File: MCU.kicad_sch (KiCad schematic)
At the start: 1 part, among them U16 STM32F303VETx

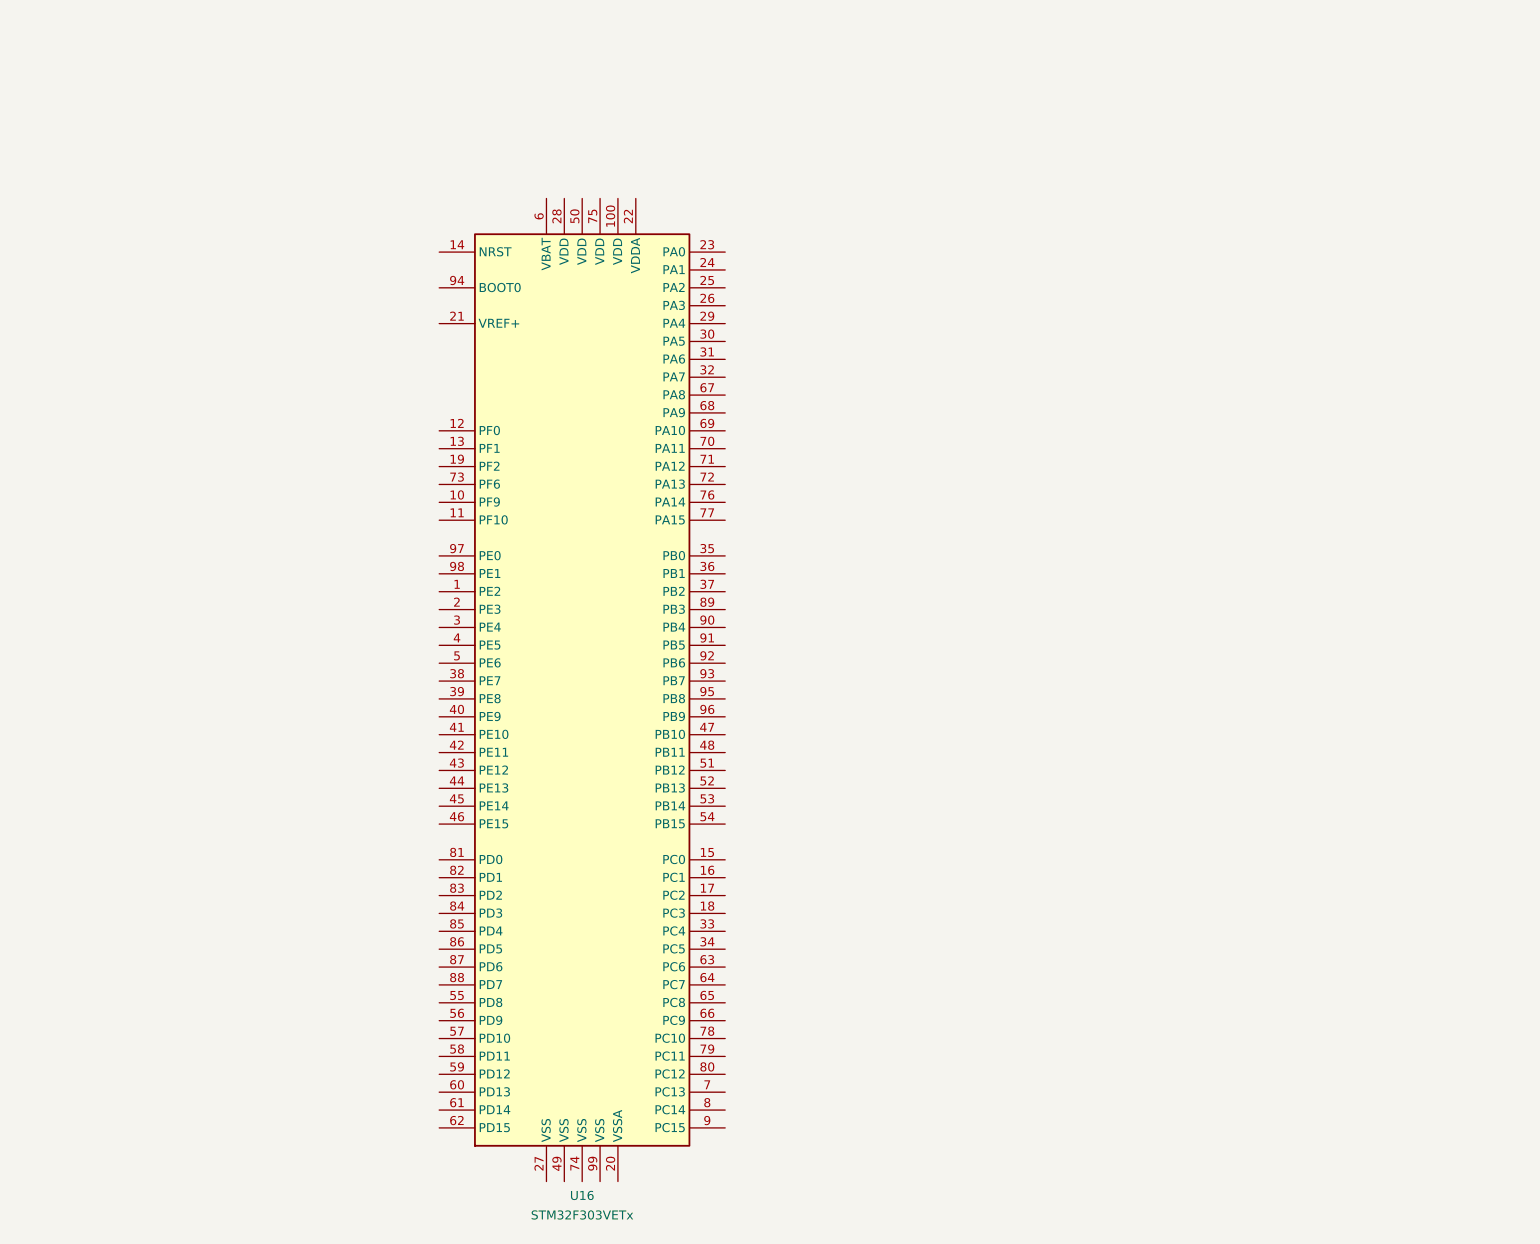
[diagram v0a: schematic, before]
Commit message: Initial layout and all parts added. Some pins still not connected to power
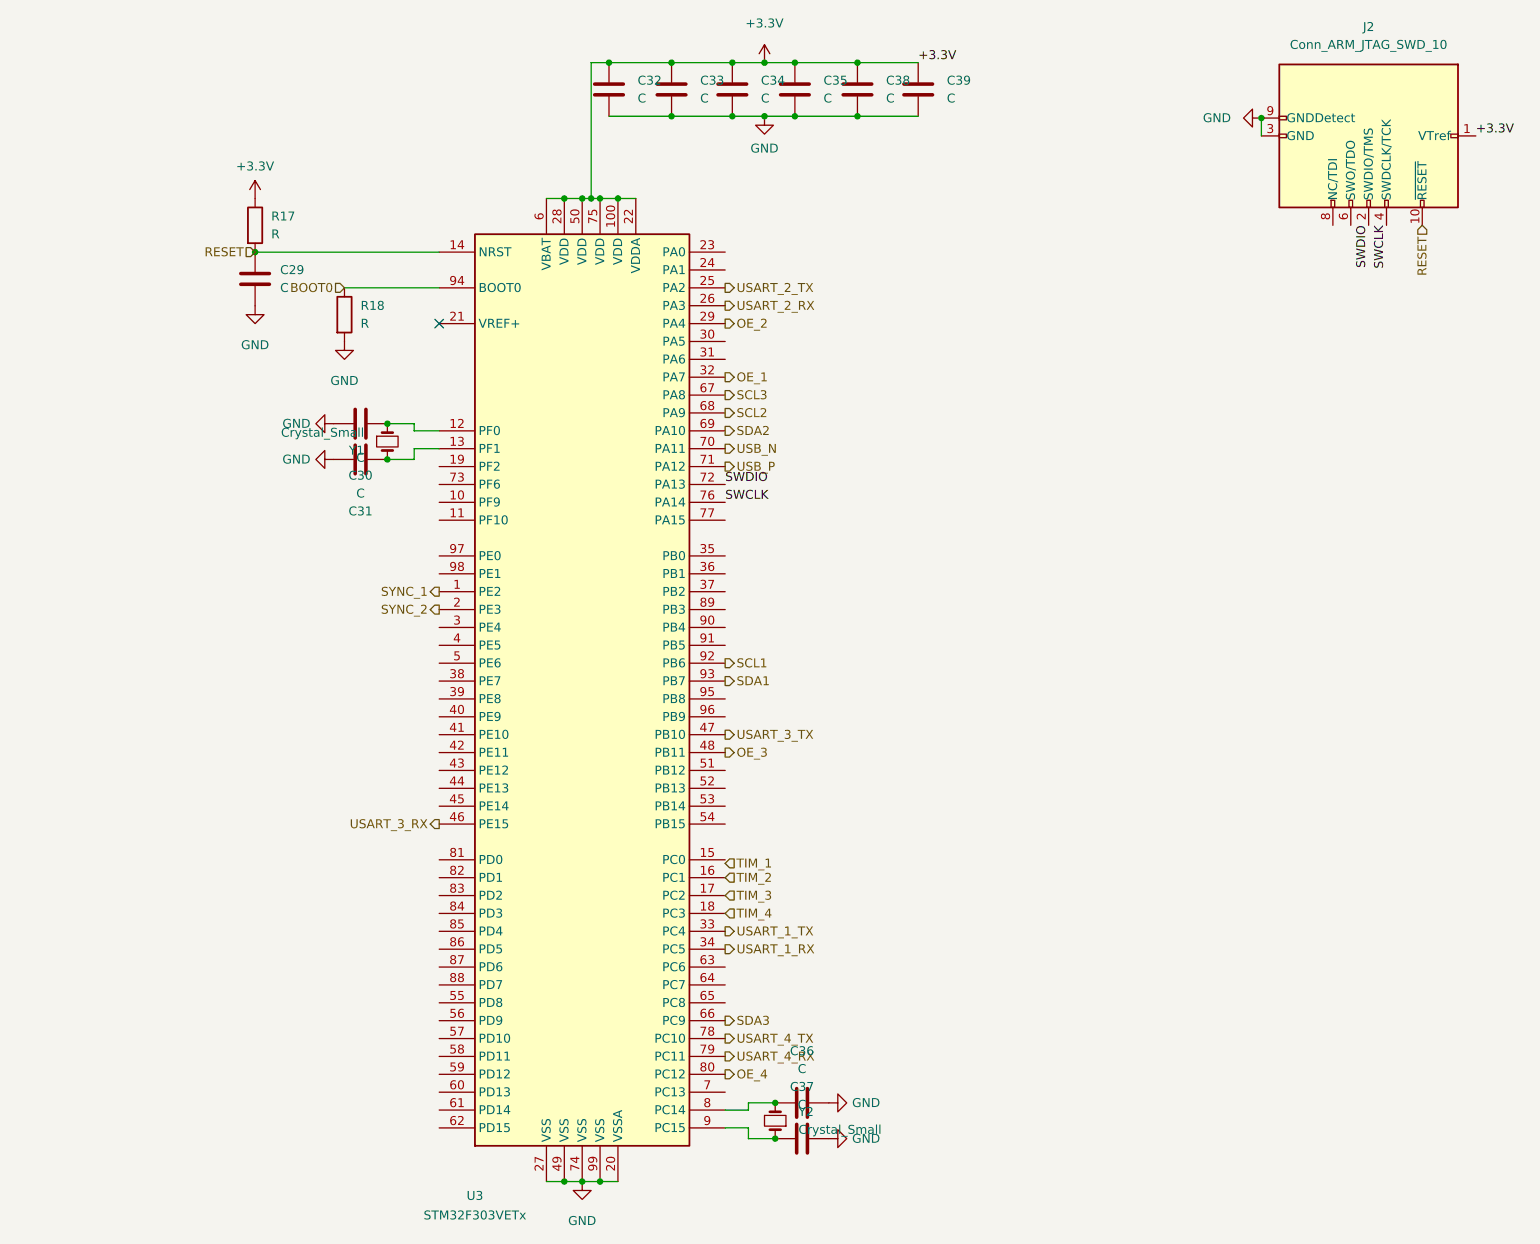
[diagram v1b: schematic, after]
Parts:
- added C29, C30, C31, C32, C33, C34, C35, C36, C37, C38, C39: C, Capacitor_SMD:C_0402_1005Metric, symbol Device:C
- added J2: Conn_ARM_JTAG_SWD_10, Connector_PinHeader_1.27mm:PinHeader_2x05_P1.27mm_Vertical_SMD, symbol Connector:Conn_ARM_JTAG_SWD_10
- added R17, R18: R, Resistor_SMD:R_0402_1005Metric, symbol Device:R
- added Y1, Y2: Crystal_Small, Crystal:Crystal_SMD_2012-2Pin_2.0x1.2mm, symbol Device:Crystal_Small
- renumbered U16 to U3
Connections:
- net SYNC_1: now reaches U3.1 (PE2)
- net +3V3: now reaches U3.100 (VDD)
- net +3V3: now also U3.22 (VDDA), U3.28 (VDD), U3.50 (VDD), U3.6 (VBAT), U3.75 (VDD), C32.1, C33.1, C34.1, C35.1, C38.1, C39.1, J2.1 (VTref), R17.1
- net at U3.12 (PF0): now also C30.1, Y1.1
- net at U3.13 (PF1): now also C31.1, Y1.2
- net RESET: now reaches U3.14 (NRST)
- net RESET: now also C29.1, J2.10 (~{RESET}), R17.2
- net TIM_2: now reaches U3.16 (PC1)
- net TIM_3: now reaches U3.17 (PC2)
- net TIM_4: now reaches U3.18 (PC3)
- net SYNC_2: now reaches U3.2 (PE3)
- net GND: now reaches U3.20 (VSSA)
- net GND: now also U3.27 (VSS), U3.49 (VSS), U3.74 (VSS), U3.99 (VSS), C29.2, C30.2, C31.2, C32.2, C33.2, C34.2, C35.2, C36.2, C37.2, C38.2, C39.2, J2.3 (GND), J2.5 (GND), J2.9 (GNDDetect), R18.2
- net USART_2_TX: now reaches U3.25 (PA2)
- net USART_2_RX: now reaches U3.26 (PA3)
- net OE_2: now reaches U3.29 (PA4)
- net OE_1: now reaches U3.32 (PA7)
- net USART_1_TX: now reaches U3.33 (PC4)
- net USART_1_RX: now reaches U3.34 (PC5)
- net USART_3_RX: now reaches U3.46 (PE15)
- net USART_3_TX: now reaches U3.47 (PB10)
- net OE_3: now reaches U3.48 (PB11)
- net SDA3: now reaches U3.66 (PC9)
- net SCL3: now reaches U3.67 (PA8)
- net SCL2: now reaches U3.68 (PA9)
- net SDA2: now reaches U3.69 (PA10)
- net USB_N: now reaches U3.70 (PA11)
- net USB_P: now reaches U3.71 (PA12)
- net SWDIO: now reaches U3.72 (PA13)
- net SWDIO: now also J2.2 (SWDIO/TMS)
- net SWCLK: now reaches U3.76 (PA14)
- net SWCLK: now also J2.4 (SWDCLK/TCK)
- net USART_4_TX: now reaches U3.78 (PC10)
- net USART_4_RX: now reaches U3.79 (PC11)
- net at U3.8 (PC14): now also C36.1, Y2.2
- net OE_4: now reaches U3.80 (PC12)
- net at U3.9 (PC15): now also C37.1, Y2.1
- net SCL1: now reaches U3.92 (PB6)
- net SDA1: now reaches U3.93 (PB7)
- net BOOT0: now reaches U3.94 (BOOT0)
- net BOOT0: now also R18.1
- no-connect marks 0 -> 1

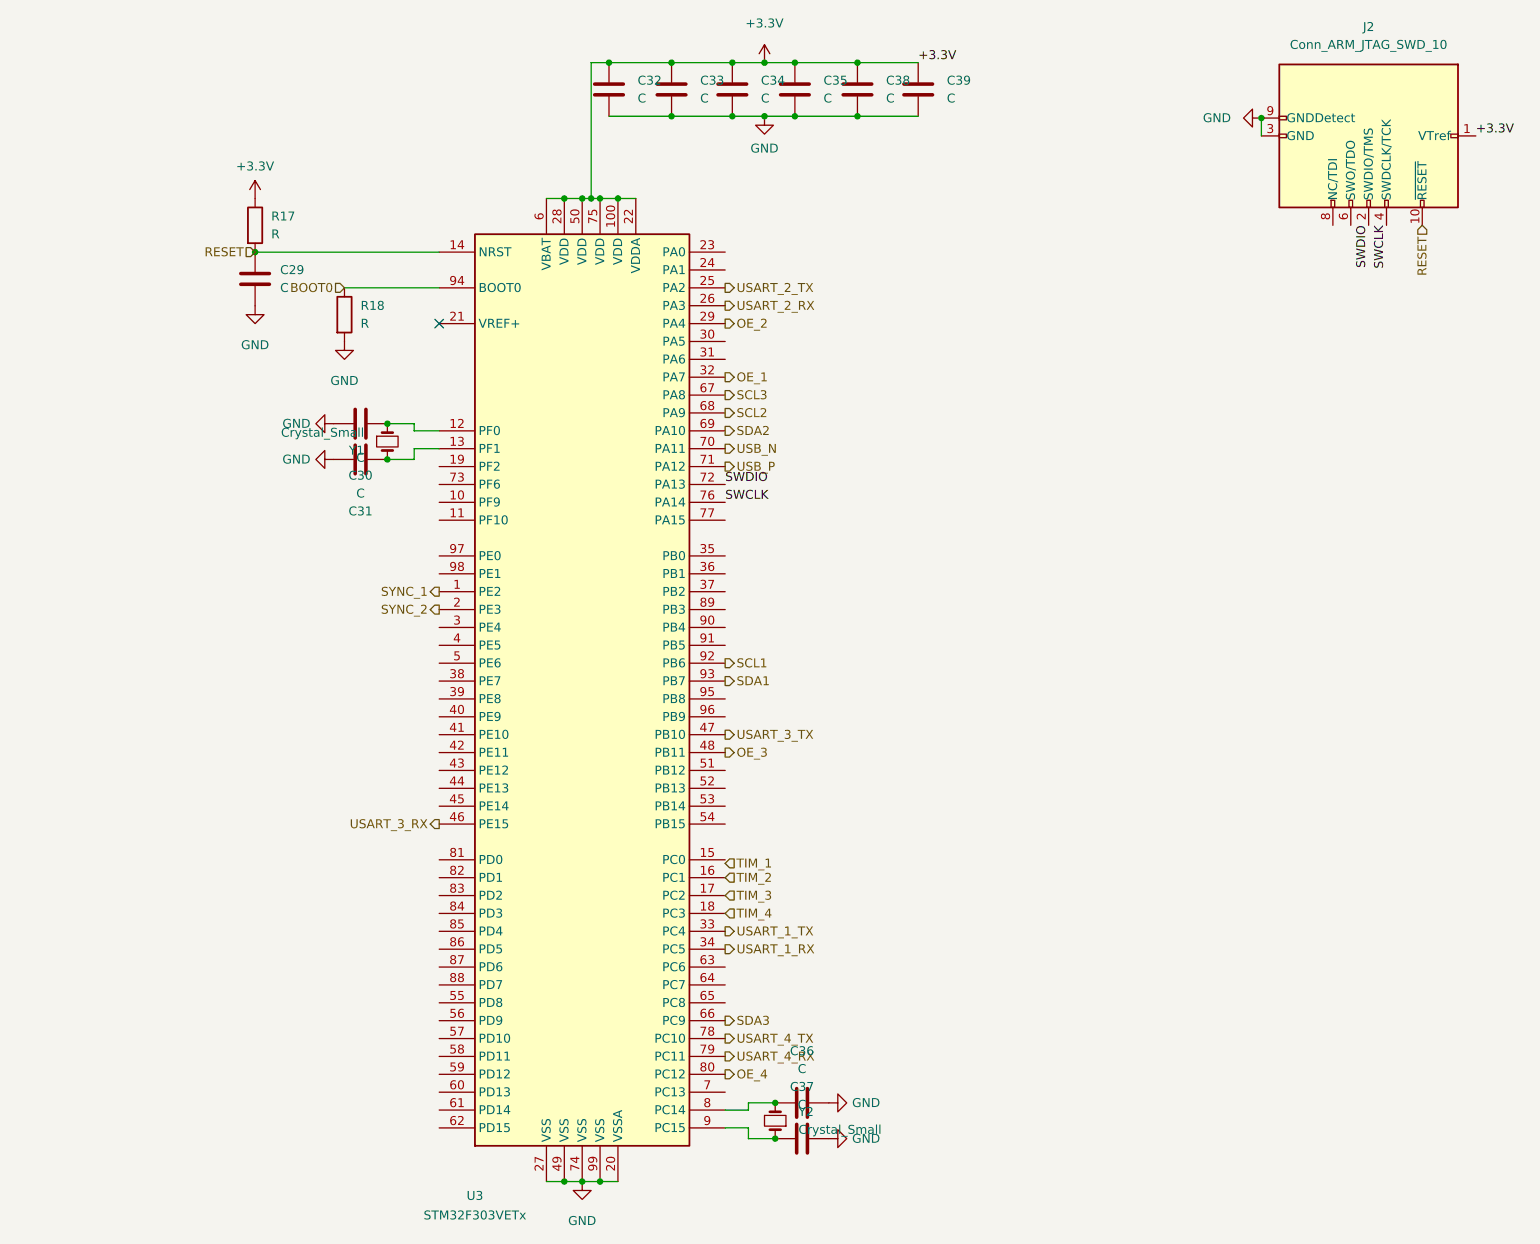
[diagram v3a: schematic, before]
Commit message: Added usb to ethernet and changed mcu to stm32g4
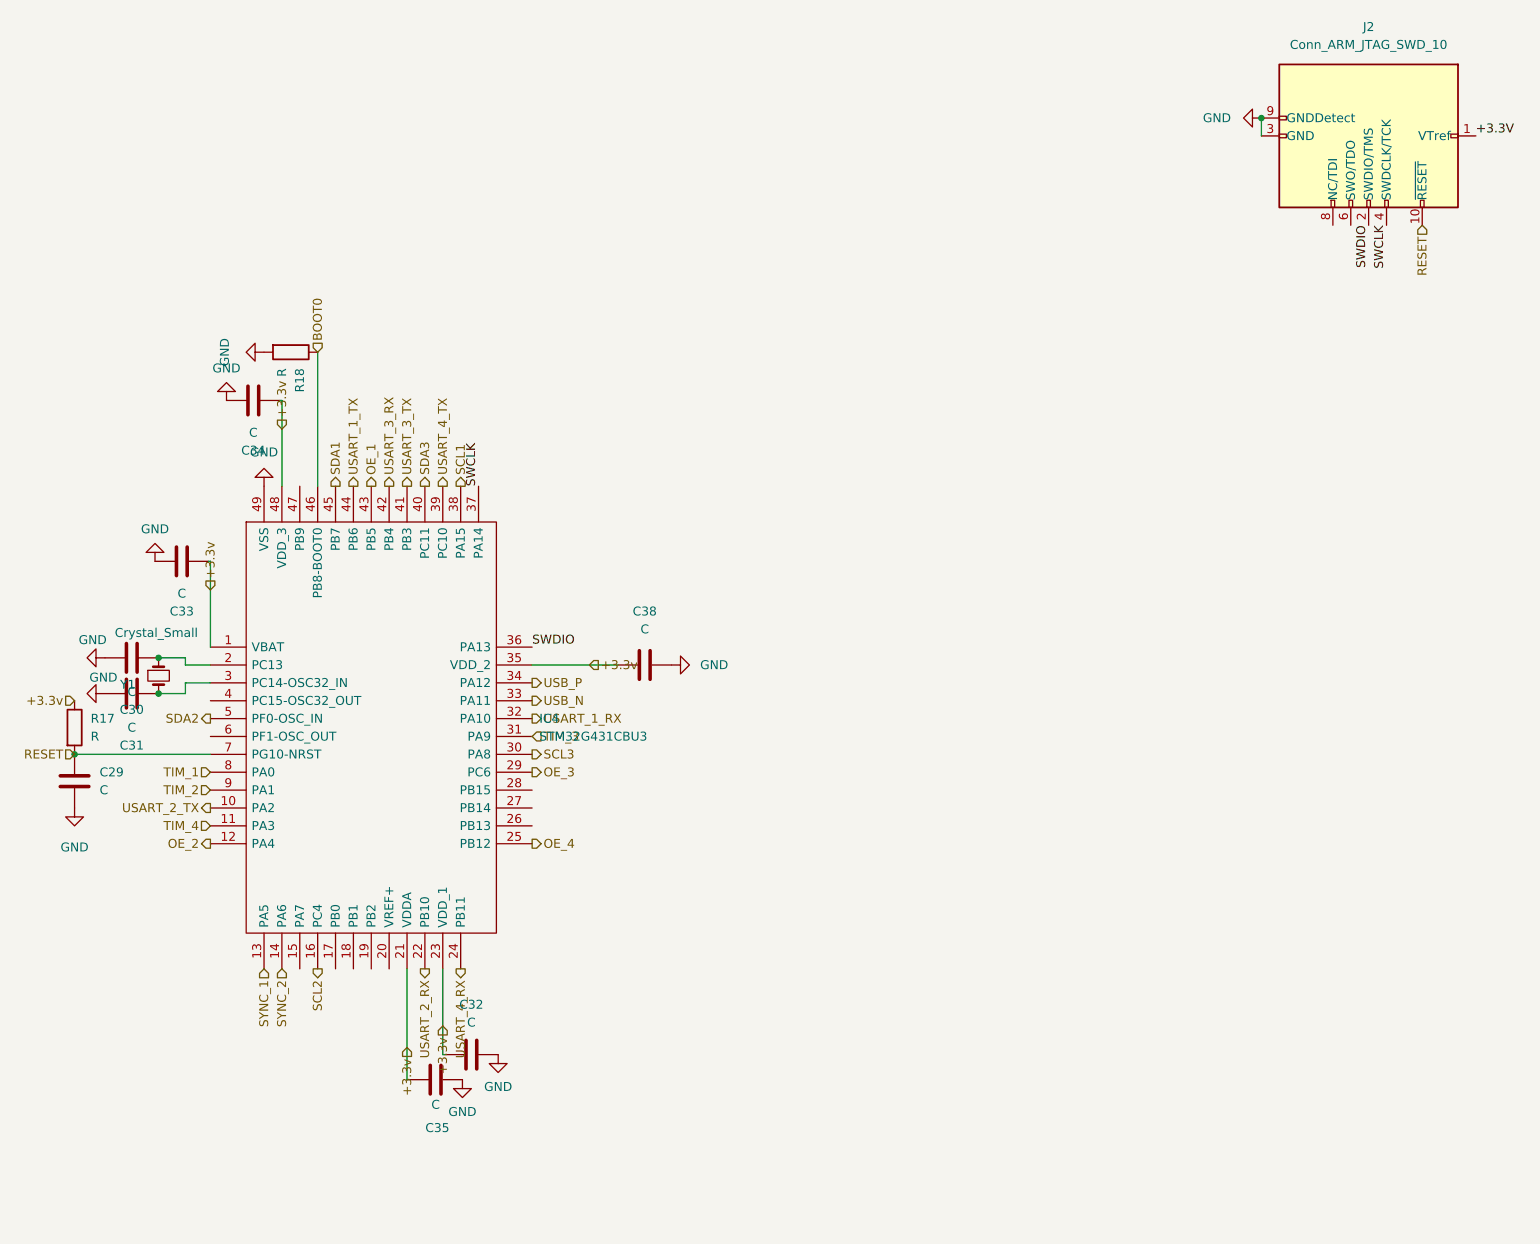
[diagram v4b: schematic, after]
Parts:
- removed C36, C37, C39: C, Capacitor_SMD:C_0402_1005Metric, symbol Device:C
- removed U3: STM32F303VETx, Package_QFP:LQFP-100_14x14mm_P0.5mm, symbol MCU_ST_STM32F3:STM32F303VETx
- removed Y2: Crystal_Small, Crystal:Crystal_SMD_2012-2Pin_2.0x1.2mm, symbol Device:Crystal_Small
- added IC4: STM32G431CBU3, STM32G431CB:QFN50P700X700X65-49N-D, symbol STM32G431CBU3:STM32G431CBU3
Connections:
- net BOOT0: now also IC4.46 (PB8-BOOT0)
- net GND: now also IC4.49 (VSS)
- net OE_1: now also IC4.43 (PB5)
- net OE_2: now also IC4.12 (PA4)
- net OE_3: now also IC4.29 (PC6)
- net OE_4: now also IC4.25 (PB12)
- net RESET: now also IC4.7 (PG10-NRST)
- net SCL1: now also IC4.38 (PA15)
- net SCL2: now also IC4.16 (PC4)
- net SCL3: now also IC4.30 (PA8)
- net SDA1: now also IC4.45 (PB7)
- net SDA2: now also IC4.5 (PF0-OSC_IN)
- net SDA3: now also IC4.40 (PC11)
- net SWCLK: now also IC4.37 (PA14)
- net SWDIO: now also IC4.36 (PA13)
- net SYNC_1: now also IC4.13 (PA5)
- net SYNC_2: now also IC4.14 (PA6)
- net TIM_1: now also IC4.8 (PA0)
- net TIM_2: now also IC4.9 (PA1)
- net TIM_3: now also IC4.31 (PA9)
- net TIM_4: now also IC4.11 (PA3)
- net USART_1_RX: now also IC4.32 (PA10)
- net USART_1_TX: now also IC4.44 (PB6)
- net USART_2_RX: now also IC4.22 (PB10)
- net USART_2_TX: now also IC4.10 (PA2)
- net USART_3_RX: now also IC4.42 (PB4)
- net USART_3_TX: now also IC4.41 (PB3)
- net USART_4_RX: now also IC4.24 (PB11)
- net USART_4_TX: now also IC4.39 (PC10)
- net USB_N: now also IC4.33 (PA11)
- net USB_P: now also IC4.34 (PA12)
- net at C30.1, Y1.1: now also IC4.2 (PC13)
- net at C31.1, Y1.2: now also IC4.3 (PC14-OSC32_IN)
- net +3V3 renamed +3.3v
- net +3.3v: now also IC4.1 (VBAT), IC4.21 (VDDA), IC4.23 (VDD_1), IC4.35 (VDD_2), IC4.48 (VDD_3); no longer J2.1 (VTref)
- new net +3.3V: J2.1 (VTref)
- no-connect marks 1 -> 0
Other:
- moved on the sheet: C29, C30, C31, C32, R17, R18, Y1
